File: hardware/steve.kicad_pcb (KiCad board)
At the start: 4 copper layers, 70 x 120 mm, 91 parts, among them J1 Conn_ARM_JTAG_SWD_10, J2 Screw_Terminal_01x04, J3 TE_1-2834015-4_Buchanan_WireM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, J4 JST-GH-6P_SM06B-GHS-TB, J5 USB_C_Receptacle_16P, J6 MicroSD_Hirose_DM3AT, Q1 Q_NMOS_GSD, SW1 SW_SPST, SW2 SW_SPST, U1 STM32F407VGTx, U2 TI_TPS51386RJNR_Regulator_Buc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, U3 TLV1117LV33DCYR, U4 BMI270, U5 BMP388/390, U6 W25Q128JVSIQ, Y1 12MHz, Y2 32.768kHz

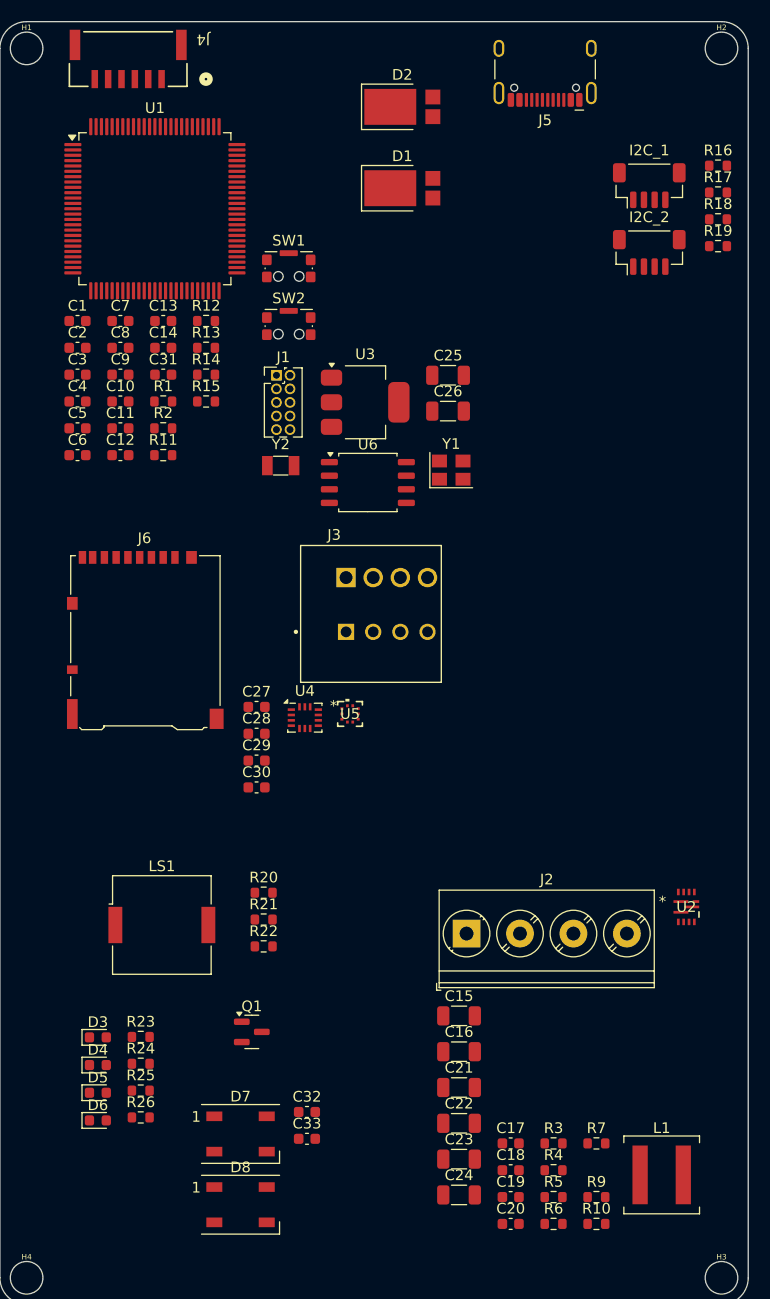
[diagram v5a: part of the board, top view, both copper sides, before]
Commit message: Removed PSM board components; added power conn; fixed telem conn
Moved PSM board components to the PSM board schematic.
Added a connector for the regulated 5V input to STEVE that comes from the PSM board.
Changed the radio telemetry connector to a 4 pin screwless terminal block to mitigate current limit concerns with the previous connector.
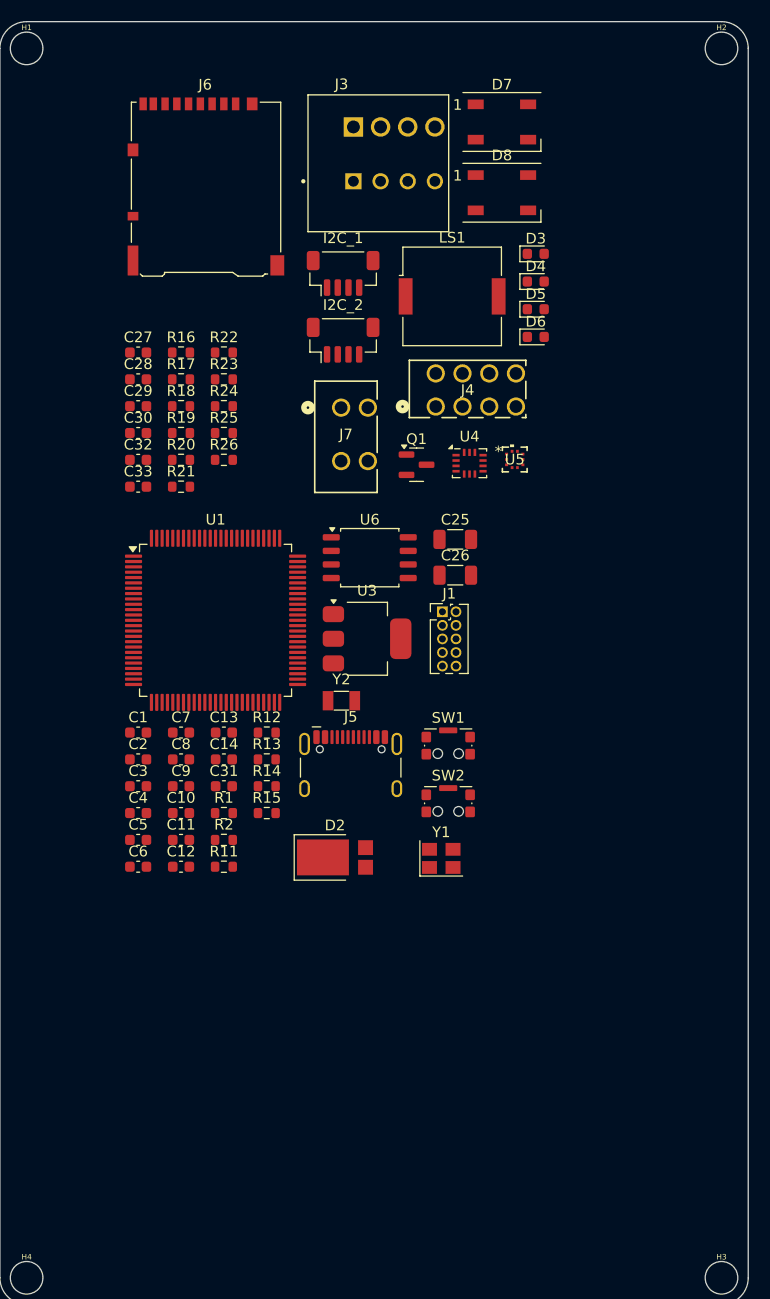
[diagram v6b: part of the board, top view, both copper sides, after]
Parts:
- removed C15, C16: 10uF, Capacitor_SMD:C_1206_3216Metric
- removed C17, C19: 0.1uF, Capacitor_SMD:C_0603_1608Metric
- removed C18: 1.0uF, Capacitor_SMD:C_0603_1608Metric
- removed C20: 22pF, Capacitor_SMD:C_0603_1608Metric
- removed C21, C22, C23, C24: 22uF, Capacitor_SMD:C_1206_3216Metric
- removed D1: Schottky Diode Array, 5A per, 40V, Imported_Footprints:PDS1040CTL-13_PowerDI-5
- removed J2: Screw_Terminal_01x04, TerminalBlock_Phoenix:TerminalBlock_Phoenix_PT-1,5-4-5.0-H_1x04_P5.00mm_Horizontal
- removed L1: 2.2uH, Inductor_SMD:L_Coilcraft_XAL6060-XXX
- removed R10: 100k 1%, Resistor_SMD:R_0603_1608Metric
- removed R3: 100k, Resistor_SMD:R_0603_1608Metric
- removed R4, R6: 0k 1%, Resistor_SMD:R_0603_1608Metric
- removed R5: 20k 1%, Resistor_SMD:R_0603_1608Metric
- removed R7: 150k 1%, Resistor_SMD:R_0603_1608Metric
- removed R9: 330k 1%, Resistor_SMD:R_0603_1608Metric
- removed U2: TI_TPS51386RJNR_Regulator_Buck_8A, Imported_Footprints:TI_TPS51386RJNR_VQFN-HR_REG_BUCK_8A
- added J7: TerminalBlock_1770885_2pos, Imported_Footprints:CONN_1814498_TerminalBlock-1770885-2pos, F.Cu at (82.8, 91.1)
- J4: value JST-GH-6P_SM06B-GHS-TB -> TerminalBlock_1770979_4pos_Vertical; footprint Imported_Footprints:CONN_JST-GH-6P_SM06B-GHS-TB -> Imported_Footprints:CONN_1814582_TerminalBlock_1770979_4pos_Vertical
- moved D7 97.8 mm to (97.0, 59.4)
- moved D8 97.8 mm to (97.0, 66.0)
- moved D6 84.0 mm to (100.1, 79.5)
- moved D3 84.0 mm to (100.1, 71.7)
- moved D4 84.0 mm to (100.1, 74.3)
- moved D5 84.0 mm to (100.1, 76.9)
- moved D2 70.5 mm to (81.3, 128.2)
- moved J5 69.5 mm to (82.8, 120.7), turned to 0 degrees
- moved LS1 64.8 mm to (92.3, 75.7)
- moved C32 63.0 mm to (62.9, 91.0)
- moved C33 63.0 mm to (62.9, 93.5)
- moved R23 62.0 mm to (71.0, 83.5)
- moved R25 62.0 mm to (71.0, 88.5)
- moved R26 62.0 mm to (71.0, 91.0)
- moved R24 62.0 mm to (71.0, 86.0)
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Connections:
- J4 pad 2: +5V -> GND
- J4 pad 3: GND -> +5V
- J4 pad 4: UART2_TX -> +5V
- J4 pad 5: UART2_RX -> UART2_TX
- J4 pad 6: GND -> UART2_TX
- J4 pad 7: (no net) -> UART2_RX
- J4 pad 8: (no net) -> UART2_RX

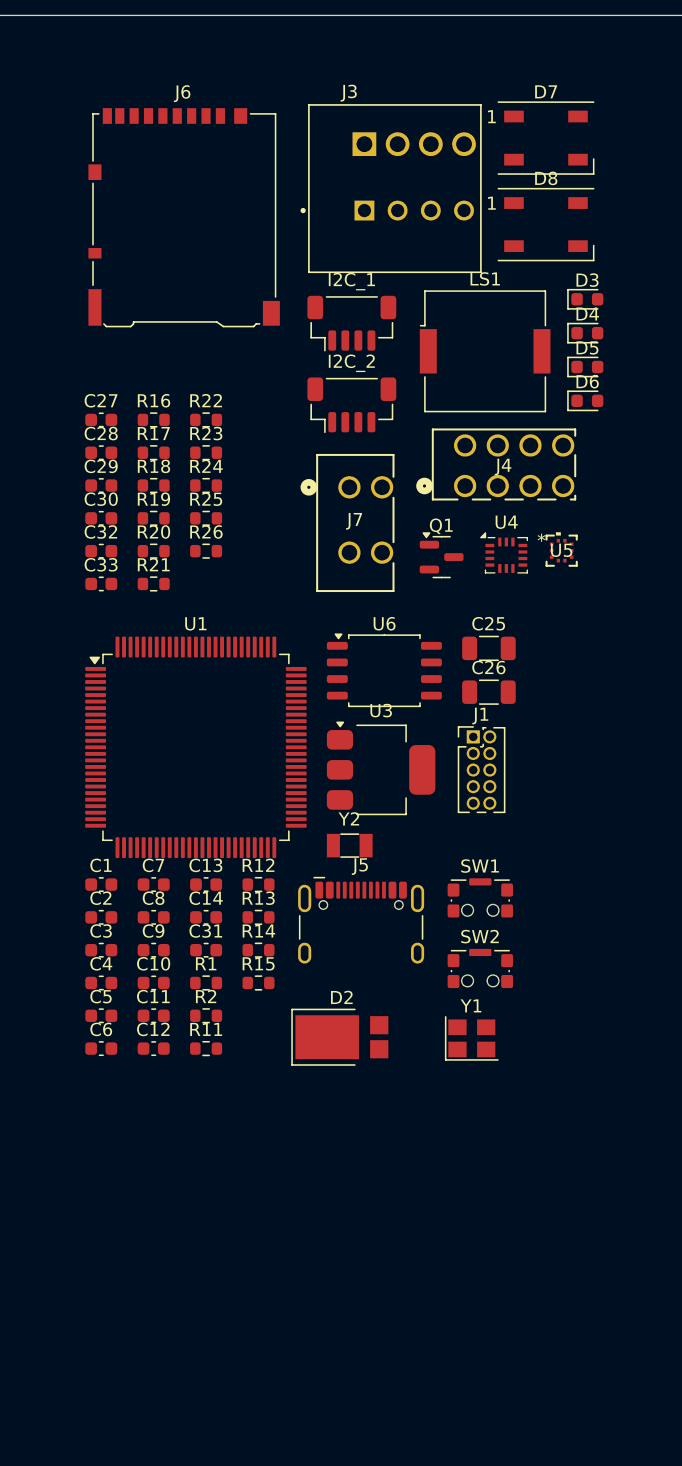
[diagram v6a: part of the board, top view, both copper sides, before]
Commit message: Finished schematic
Finished schematic - 3D model fixes using custom imports, all important parts sourced, additional GPIO/bus pins broken out, PSM board signals broken out, battery voltage sense line added.
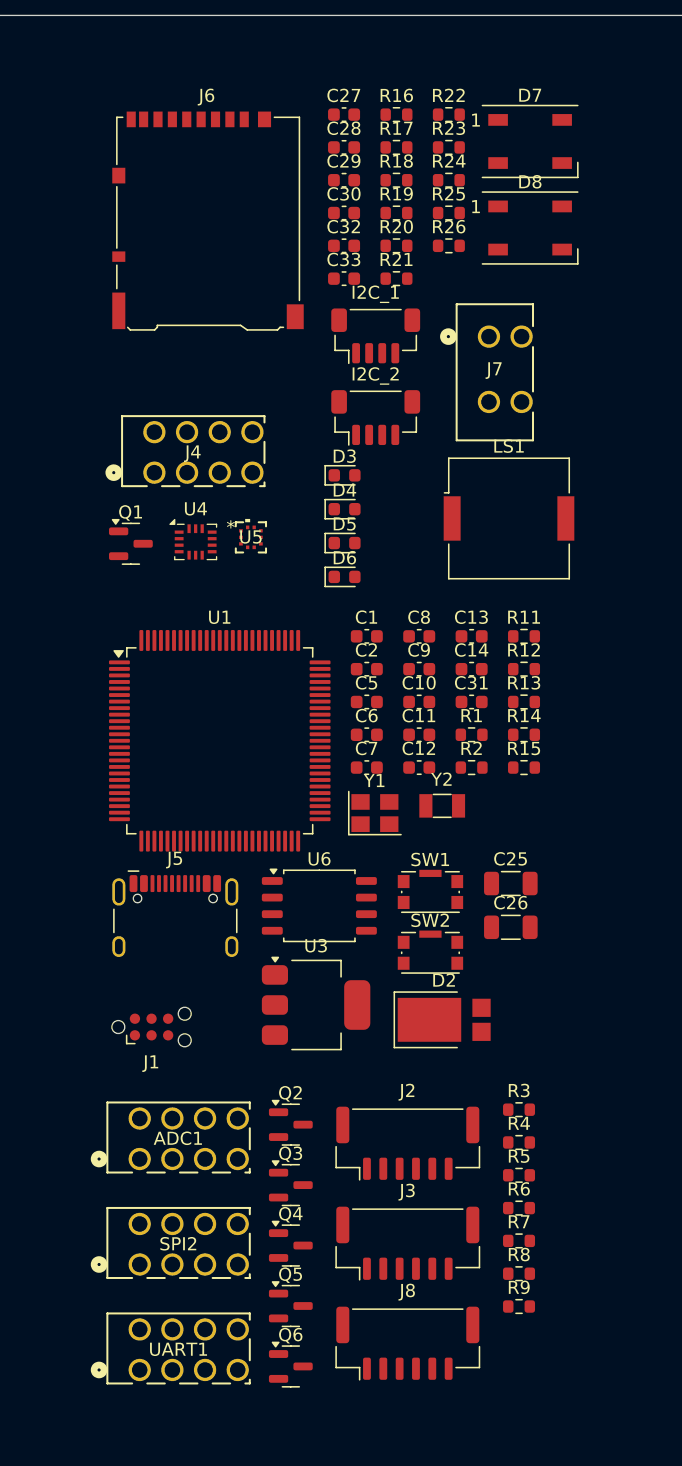
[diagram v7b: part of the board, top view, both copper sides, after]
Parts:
- removed C3, C4: 22pF, Capacitor_SMD:C_0603_1608Metric
- added ADC1: TerminalBlock_1770979_4pos_Vertical, Imported_Footprints:CONN_1814582_TerminalBlock_1770979_4pos_Vertical, F.Cu at (71.8, 134.4)
- added J2: Conn_01x06, Connector_JST:JST_GH_BM06B-GHS-TBT_1x06-1MP_P1.25mm_Vertical, F.Cu at (86.4, 136.3)
- added J8: Conn_01x06, Connector_JST:JST_GH_BM06B-GHS-TBT_1x06-1MP_P1.25mm_Vertical, F.Cu at (86.4, 151.6)
- added Q2: Q_NMOS_GSD, Package_TO_SOT_SMD:SOT-23, F.Cu at (77.4, 134.9)
- added Q3: Q_NMOS_GSD, Package_TO_SOT_SMD:SOT-23, F.Cu at (77.4, 139.5)
- added Q4: Q_NMOS_GSD, Package_TO_SOT_SMD:SOT-23, F.Cu at (77.4, 144.1)
- added Q5: Q_NMOS_GSD, Package_TO_SOT_SMD:SOT-23, F.Cu at (77.4, 148.7)
- added Q6: Q_NMOS_GSD, Package_TO_SOT_SMD:SOT-23, F.Cu at (77.4, 153.4)
- added R3: 10k, Resistor_SMD:R_0603_1608Metric, F.Cu at (94.9, 133.7)
- added R4: 10k, Resistor_SMD:R_0603_1608Metric, F.Cu at (94.9, 136.2)
- added R5: 10k, Resistor_SMD:R_0603_1608Metric, F.Cu at (94.9, 138.7)
- added R6: 10k, Resistor_SMD:R_0603_1608Metric, F.Cu at (94.9, 141.3)
- added R7: 10k, Resistor_SMD:R_0603_1608Metric, F.Cu at (94.9, 143.8)
- added R8: 422k 1%, Resistor_SMD:R_0603_1608Metric, F.Cu at (94.9, 146.3)
- added R9: 100k 0.5%, Resistor_SMD:R_0603_1608Metric, F.Cu at (94.9, 148.8)
- added SPI2: TerminalBlock_1770979_4pos_Vertical, Imported_Footprints:CONN_1814582_TerminalBlock_1770979_4pos_Vertical, F.Cu at (71.8, 142.5)
- added UART1: TerminalBlock_1770979_4pos_Vertical, Imported_Footprints:CONN_1814582_TerminalBlock_1770979_4pos_Vertical, F.Cu at (71.8, 150.5)
- C5, C6: value 15pF -> 5pF
- J1: value Conn_ARM_JTAG_SWD_10 -> Conn_ARM_SWD_TagConnect_TC2030-NL; footprint Connector_PinHeader_1.27mm:PinHeader_2x05_P1.27mm_Vertical -> Connector:Tag-Connect_TC2030-IDC-NL_2x03_P1.27mm_Vertical
- J3: value TE_1-2834015-4_Buchanan_WireMate_Screwless_Terminal_Block -> Conn_01x06; footprint Imported_Footprints:TE_1-2834015-4_Buchanan_WireMate_Screwless_Terminal_Block -> Connector_JST:JST_GH_BM06B-GHS-TBT_1x06-1MP_P1.25mm_Vertical
- J5: footprint Connector_USB:USB_C_Receptacle_HCTL_HC-TYPE-C-16P-01A -> Imported_Footprints:USB_C_Receptacle_3D_HCTL_HC-TYPE-C-16P-01A
- J6: footprint Connector_Card:microSD_HC_Hirose_DM3AT-SF-PEJM5 -> Imported_Footprints:microSD_3D_HC_Hirose_DM3AT-SF-PEJM5
- SW1, SW2: value SW_SPST -> KMR221G; footprint Button_Switch_SMD:SW_SPST_CK_KMS2xxGP -> Imported_Footprints:SW_Push_3D_1P1T-SH_NO_CK_KMR2xxG
- U6: footprint Package_SO:SOIC-8_5.23x5.23mm_P1.27mm -> Imported_Footprints:SOIC-8_5.23x5.23mm_P1.27mm_3D
- Y1: value 12MHz -> 8MHz
- moved J3 81.6 mm to (86.4, 143.9)
- moved R11 39.8 mm to (95.3, 97.5)
- moved J1 33.1 mm to (66.8, 127.4)
- moved C5 31.5 mm to (83.2, 102.5)
- moved C6 31.5 mm to (83.2, 105.0)
- moved C27 29.8 mm to (81.5, 57.6)
- moved C29 29.8 mm to (81.5, 62.6)
- moved C30 29.8 mm to (81.5, 65.1)
- moved C32 29.8 mm to (81.5, 67.6)
- moved C33 29.8 mm to (81.5, 70.1)
- moved R16 29.8 mm to (85.5, 57.6)
- moved R18 29.8 mm to (85.5, 62.6)
- moved R19 29.8 mm to (85.5, 65.1)
- moved R20 29.8 mm to (85.5, 67.6)
- moved R21 29.8 mm to (85.5, 70.1)
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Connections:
- C1 pad 2: GND -> HSE_OSC_IN
- C10 pad 2: GND -> HSE_OSC_IN
- C11 pad 2: GND -> HSE_OSC_IN
- C12 pad 2: GND -> HSE_OSC_IN
- C13 pad 2: GND -> HSE_OSC_IN
- C14 pad 2: GND -> HSE_OSC_IN
- C2 pad 2: GND -> HSE_OSC_IN
- C25 pad 2: GND -> HSE_OSC_IN
- C26 pad 2: GND -> HSE_OSC_IN
- C27 pad 2: GND -> HSE_OSC_IN
- C28 pad 2: GND -> HSE_OSC_IN
- C29 pad 2: GND -> HSE_OSC_IN
- C30 pad 2: GND -> HSE_OSC_IN
- C31 pad 2: GND -> HSE_OSC_IN
- C32 pad 2: GND -> HSE_OSC_IN
- C33 pad 2: GND -> HSE_OSC_IN
- C5 pad 2: GND -> HSE_OSC_IN
- C6 pad 2: GND -> HSE_OSC_IN
- C7 pad 2: GND -> HSE_OSC_IN
- C8 pad 2: GND -> HSE_OSC_IN
- C9 pad 2: GND -> HSE_OSC_IN
- D3 pad 1: GND -> HSE_OSC_IN
- D4 pad 1: GND -> HSE_OSC_IN
- D5 pad 1: GND -> HSE_OSC_IN
- D6 pad 1: GND -> HSE_OSC_IN
- D7 pad 3: GND -> HSE_OSC_IN
- D8 pad 3: GND -> HSE_OSC_IN
- I2C_1 pad 1: GND -> HSE_OSC_IN
- I2C_2 pad 1: GND -> HSE_OSC_IN
- J1 pad 3: GND -> ~{RESET}
- J1 pad 5: GND -> HSE_OSC_IN
- J4 pad 1: GND -> HSE_OSC_IN
- J4 pad 2: GND -> HSE_OSC_IN
- J5 pad A1: GND -> HSE_OSC_IN
- J5 pad A12: GND -> HSE_OSC_IN
- J5 pad B1: GND -> HSE_OSC_IN
- J5 pad B12: GND -> HSE_OSC_IN
- J5 pad S1: GND -> HSE_OSC_IN
- J6 pad 11: GND -> HSE_OSC_IN
- J6 pad 6: GND -> HSE_OSC_IN
- J7 pad 3: GND -> HSE_OSC_IN
- J7 pad 4: GND -> HSE_OSC_IN
- Q1 pad 2: GND -> HSE_OSC_IN
- R1 pad 2: GND -> HSE_OSC_IN
- R13 pad 2: GND -> HSE_OSC_IN
- R14 pad 2: GND -> HSE_OSC_IN
- SW1 pad 1: BOOT0 -> ~{RESET}
- SW1 pad 2: +3.3V -> HSE_OSC_IN
- SW1 pad SH: (no net) -> HSE_OSC_IN
- SW2 pad 1: ~{RESET} -> +3.3V
- SW2 pad 2: GND -> BOOT0
- SW2 pad SH: (no net) -> HSE_OSC_IN
- U1 pad 1: unconnected-(U1-PE2-Pad1) -> MOSFET_3
- U1 pad 10: GND -> HSE_OSC_IN
- U1 pad 13: HSE_OSC_OUT -> HSE_OSC_IN
- U1 pad 15: unconnected-(U1-PC0-Pad15) -> ADC_C0
- U1 pad 16: unconnected-(U1-PC1-Pad16) -> ADC_C1
- U1 pad 2: unconnected-(U1-PE3-Pad2) -> MOSFET_4
- U1 pad 20: GND -> HSE_OSC_IN
- U1 pad 27: GND -> HSE_OSC_IN
- U1 pad 3: unconnected-(U1-PE4-Pad3) -> MOSFET_5
- U1 pad 33: unconnected-(U1-PC4-Pad33) -> BATT1_V_ADC
- U1 pad 39: unconnected-(U1-PE8-Pad39) -> SERVO_PWM_1
- U1 pad 41: unconnected-(U1-PE10-Pad41) -> SERVO_PWM_2
- U1 pad 43: unconnected-(U1-PE12-Pad43) -> SERVO_PWM_3
- U1 pad 45: unconnected-(U1-PE14-Pad45) -> SERVO_PWM_4
- U1 pad 68: unconnected-(U1-PA9-Pad68) -> UART1_TX_PWM_A9
- U1 pad 69: unconnected-(U1-PA10-Pad69) -> UART1_RX_PWM_A10
- U1 pad 74: GND -> HSE_OSC_IN
- U1 pad 84: unconnected-(U1-PD3-Pad84) -> CONT1
- U1 pad 85: unconnected-(U1-PD4-Pad85) -> CONT2
- U1 pad 86: unconnected-(U1-PD5-Pad86) -> CONT3
- U1 pad 87: unconnected-(U1-PD6-Pad87) -> CONT4
- U1 pad 88: unconnected-(U1-PD7-Pad88) -> CONT5
- U1 pad 97: unconnected-(U1-PE0-Pad97) -> MOSFET_1
- U1 pad 98: unconnected-(U1-PE1-Pad98) -> MOSFET_2
- U1 pad 99: GND -> HSE_OSC_IN
- U3 pad 1: GND -> HSE_OSC_IN
- U4 pad 6: GND -> HSE_OSC_IN
- U4 pad 7: GND -> HSE_OSC_IN
- U5 pad 3: GND -> HSE_OSC_IN
- U5 pad 8: GND -> HSE_OSC_IN
- U5 pad 9: GND -> HSE_OSC_IN
- U6 pad 4: GND -> HSE_OSC_IN
- Y1 pad 2: GND -> HSE_OSC_IN
- Y1 pad 3: HSE_OSC_OUT -> HSE_OSC_IN
- Y1 pad 4: GND -> HSE_OSC_IN
